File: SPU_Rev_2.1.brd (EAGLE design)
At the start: 127.6 x 101.6 mm, 251 parts, among them Q1 12MHz

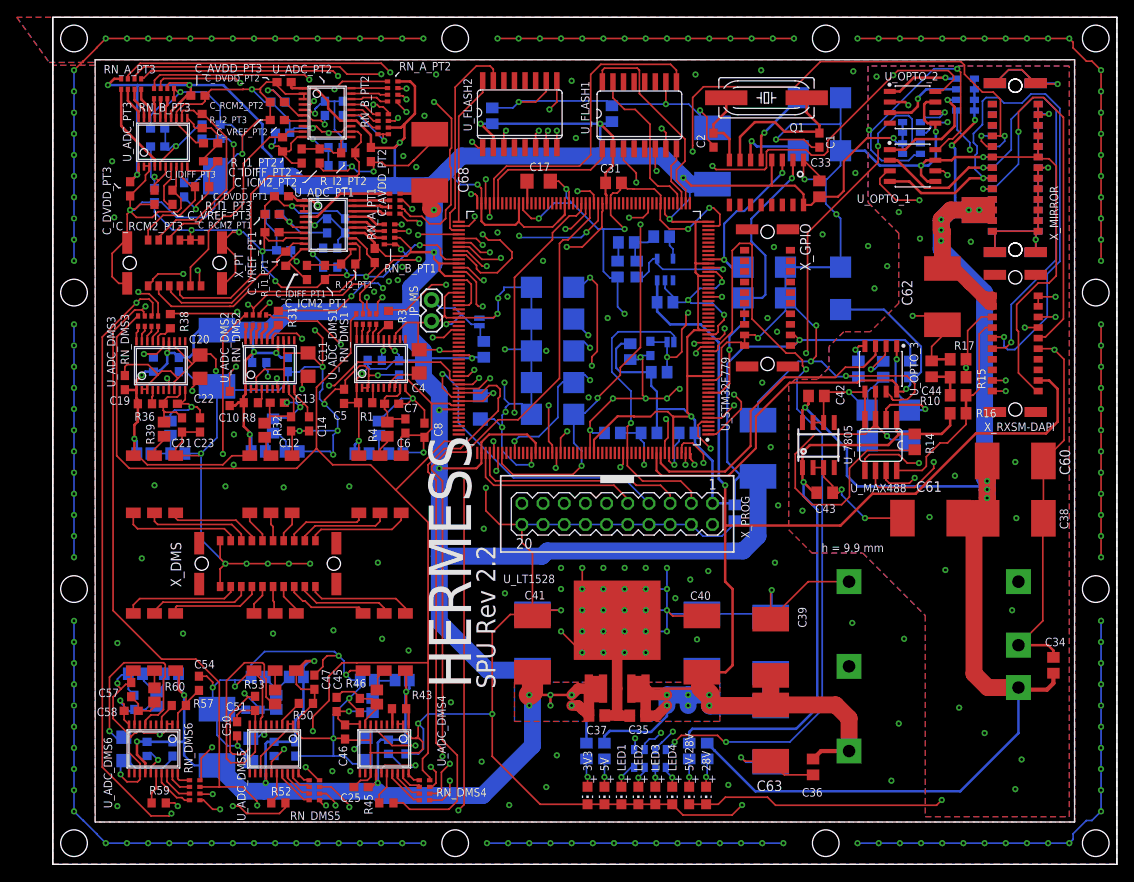
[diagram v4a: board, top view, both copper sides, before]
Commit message: microsd added
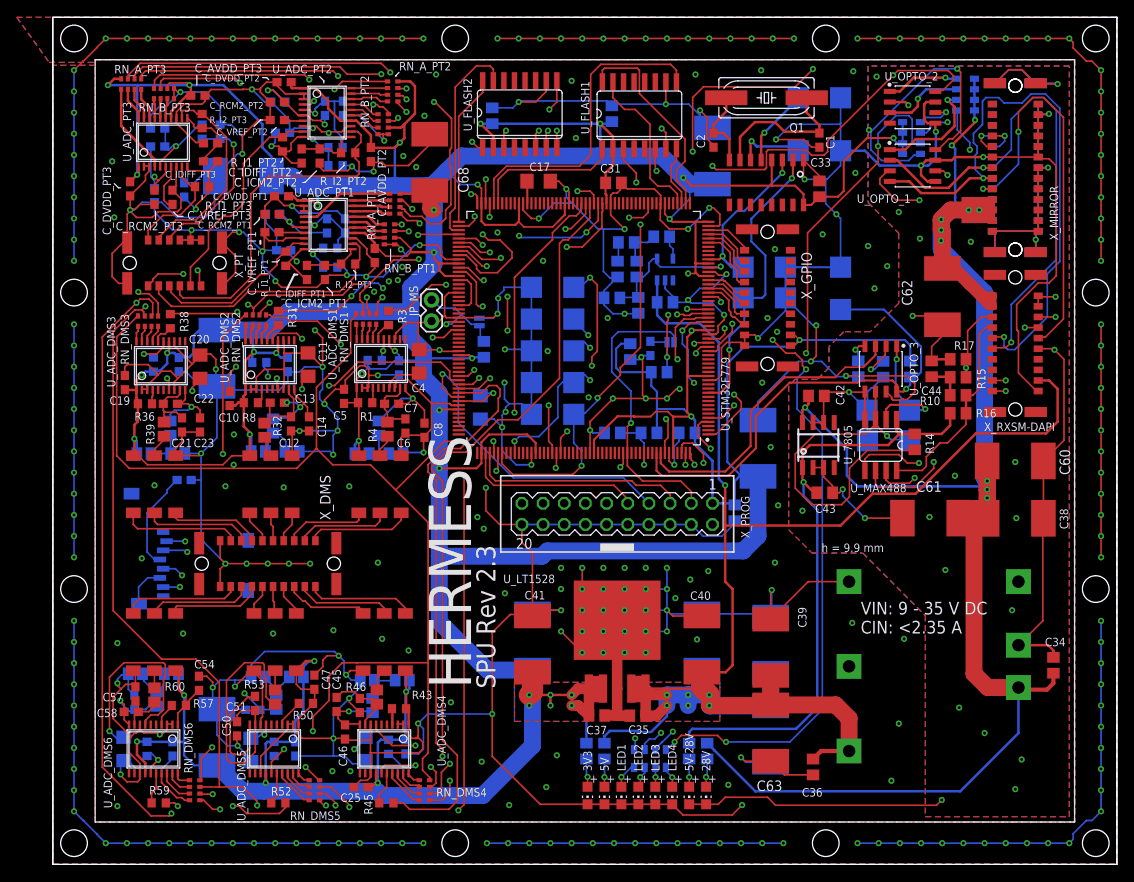
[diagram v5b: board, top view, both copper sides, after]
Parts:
- added C74: 10n, rcl:C0805
- added C75: 100n, rcl:C0805
- added C76: 100n, aSparkFun:0603-CAP
- added U$7: MICROSD, adafruit:MICROSD
- moved C57 0.72 mm to (15.0, 20.4)
- moved C58 0.13 mm to (14.5, 18.3)
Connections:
- new net IO1: U_STM32F779.50, X_GPIO.P$A10
- new net IO2: U_STM32F779.49, X_GPIO.P$A9
- new net IO3: U_STM32F779.48, X_GPIO.P$A8
- new net IO4: U_STM32F779.47, X_GPIO.P$A7
- new net IO5: U_STM32F779.38, X_GPIO.P$A6
- new net IO6: U_STM32F779.37, X_GPIO.P$A5
- new net IO7: U_STM32F779.36, X_GPIO.P$A4
- new net IO8: U_STM32F779.35, X_GPIO.P$A3
- new net SD_CS: U$7.2, U_STM32F779.31
- new net SPI5_MISO: U$7.7, U_STM32F779.29
- new net SPI5_MOSI: U$7.3, U_STM32F779.30
- new net SPI5_SCK: U$7.5, U_STM32F779.28
- net 3V3: now also C76.1, U$7.4
- net 3V3REF: now also C74.2, C75.2
- net GND: now also C74.1, C75.1, C76.2, U$7.6, U$7.MT1, U$7.MT2
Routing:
- net SPI5_SCK: track 0.00 -> 95.4 mm, vias 0 -> 3
- net SPI5_MISO: track 0.00 -> 89.1 mm, vias 0 -> 3
- net SD_CS: track 0.00 -> 82.4 mm, vias 0 -> 2
- net SPI5_MOSI: track 0.00 -> 82.4 mm, vias 0 -> 2
- net LED_4: track 98.8 -> 81.3 mm, vias 3 -> 5
- net 3V3: track 862.8 -> 877.4 mm, vias 39 -> 41
- net GND: track 1440.1 -> 1454.0 mm
- net IO4: track 0.00 -> 7.74 mm
- net IO8: track 0.00 -> 6.83 mm
- net IO3: track 0.00 -> 6.78 mm
- net IO7: track 0.00 -> 6.36 mm
- net IO2: track 0.00 -> 6.26 mm
- net IO1: track 0.00 -> 5.57 mm
- net IO6: track 0.00 -> 5.33 mm
- net IO5: track 0.00 -> 4.96 mm
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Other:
- board text added: "SPU Rev 2.3"
- board text added: "VIN: 9 - 35 V DC CIN: <2.35 A"
- board text removed: "SPU Rev 2.2"

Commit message: foo
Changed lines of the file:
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@@
 <drawing>
 <settings>
-<setting alwaysvectorfont="no"/>
+<setting alwaysvectorfont="yes"/>
 <setting verticaltext="up"/>
 </settings>
@@
 <wire x1="15.416" y1="30.783" x2="15.416" y2="31.261" width="0.2032" layer="16"/>
 <wire x1="16.454" y1="34.361" x2="15.367" y2="33.274" width="0.2032" layer="16"/>
-<wire x1="99.568" y1="91.948" x2="101.092" y2="95.123" width="0" layer="19" extent="16-16"/>
-<wire x1="64.4398" y1="61.5696" x2="62.484" y2="61.595" width="0" layer="19" extent="16-16"/>
-<wire x1="40.767" y1="11.176" x2="41.187" y2="9.271" width="0" layer="19" extent="1-1"/>
-<wire x1="71.628" y1="65.532" x2="73.66" y2="66.04" width="0" layer="19" extent="1-1"/>
-<wire x1="12.446" y1="77.597" x2="14.351" y2="78.486" width="0" layer="19" extent="1-1"/>
-<wire x1="38.608" y1="11.176" x2="40.767" y2="11.176" width="0" layer="19" extent="1-1"/>
-<wire x1="91.948" y1="63.881" x2="89.662" y2="63.119" width="0" layer="19" extent="1-1"/>
-<wire x1="90.805" y1="65.532" x2="91.948" y2="63.881" width="0" layer="19" extent="1-1"/>
-<wire x1="91.694" y1="73.787" x2="92.964" y2="71.628" width="0" layer="19" extent="16-16"/>
-<wire x1="97.409" y1="75.565" x2="99.06" y2="77.978" width="0" layer="19" extent="1-1"/>
-<wire x1="86.106" y1="9.525" x2="87.757" y2="7.112" width="0" layer="19" extent="1-1"/>
-<wire x1="67.31" y1="93.98" x2="64.262" y2="94.0054" width="0" layer="19" extent="1-1"/>
-<wire x1="38.735" y1="28.067" x2="39.37" y2="25.019" width="0" layer="19" extent="1-1"/>
-<wire x1="101.346" y1="82.931" x2="99.568" y2="85.598" width="0" layer="19" extent="16-16"/>
-<wire x1="91.694" y1="36.195" x2="91.313" y2="32.893" width="0" layer="19" extent="1-1"/>
-<wire x1="63.881" y1="72.39" x2="62.484" y2="69.215" width="0" layer="19" extent="16-16"/>
-<wire x1="91.186" y1="50.038" x2="89.662" y2="53.286" width="0" layer="19" extent="16-16"/>
-<wire x1="82.169" y1="94.742" x2="78.613" y2="93.8784" width="0" layer="19" extent="1-1"/>
-<wire x1="12.827" y1="26.543" x2="14.732" y2="23.239" width="0" layer="19" extent="1-1"/>
-<wire x1="12.827" y1="6.985" x2="13.208" y2="10.795" width="0" layer="19" extent="1-1"/>
-<wire x1="12.192" y1="84.328" x2="16.013" y2="83.6962" width="0" layer="19" extent="1-1"/>
-<wire x1="32.766" y1="45.212" x2="33.782" y2="49.024" width="0" layer="19" extent="1-1"/>
-<wire x1="26.797" y1="51.562" x2="22.733" y2="51.855" width="0" layer="19" extent="1-1"/>
-<wire x1="59.309" y1="32.512" x2="62.611" y2="30.045" width="0" layer="19" extent="16-16"/>
-<wire x1="102.87" y1="74.168" x2="99.568" y2="71.628" width="0" layer="19" extent="16-16"/>
-<wire x1="105.156" y1="71.755" x2="102.87" y2="74.168" width="0" layer="19" extent="1-1"/>
-<wire x1="103.632" y1="69.088" x2="105.156" y2="71.755" width="0" layer="19" extent="1-1"/>
-<wire x1="25.781" y1="45.339" x2="21.678" y2="46.101" width="0" layer="19" extent="16-16"/>
-<wire x1="40.64" y1="45.339" x2="38.7096" y2="49.149" width="0" layer="19" extent="1-1"/>
-<wire x1="17.272" y1="45.466" x2="19.812" y2="49.024" width="0" layer="19" extent="1-1"/>
-<wire x1="14.516" y1="44.461" x2="17.272" y2="45.466" width="0" layer="19" extent="16-16"/>
-<wire x1="44.577" y1="27.051" x2="42.291" y2="23.239" width="0" layer="19" extent="1-1"/>
-<wire x1="47.752" y1="25.654" x2="44.577" y2="27.051" width="0" layer="19" extent="1-1"/>
-<wire x1="90.17" y1="57.785" x2="89.662" y2="53.286" width="0" layer="19" extent="16-16"/>
-<wire x1="56.769" y1="40.259" x2="61.341" y2="40.767" width="0" layer="19" extent="1-1"/>
-<wire x1="52.832" y1="19.431" x2="48.895" y2="16.891" width="0" layer="19" extent="1-1"/>
-<wire x1="100.965" y1="28.956" x2="100.584" y2="33.909" width="0" layer="19" extent="1-1"/>
-<wire x1="83.693" y1="35.179" x2="78.74" y2="35.56" width="0" layer="19" extent="1-1"/>
-<wire x1="31.496" y1="27.686" x2="29.21" y2="23.239" width="0" layer="19" extent="1-1"/>
-<wire x1="64.262" y1="9.271" x2="69.215" y2="7.205" width="0" layer="19" extent="1-1"/>
-<wire x1="65.532" y1="13.081" x2="64.262" y2="9.271" width="0" layer="19" extent="1-1"/>
-<wire x1="59.817" y1="7.112" x2="64.262" y2="9.271" width="0" layer="19" extent="1-1"/>
-<wire x1="15.416" y1="31.261" x2="12.827" y2="26.543" width="0" layer="19" extent="16-16"/>
-<wire x1="15.748" y1="36.703" x2="17.916" y2="34.361" width="0" layer="19" extent="16-16"/>
-<wire x1="20.701" y1="27.686" x2="22.606" y2="22.567" width="0" layer="19" extent="1-1"/>
-<wire x1="92.075" y1="43.053" x2="86.868" y2="41.214" width="0" layer="19" extent="16-16"/>
-<wire x1="56.515" y1="12.319" x2="57.785" y2="18.034" width="0" layer="19" extent="1-1"/>
-<wire x1="107.188" y1="27.051" x2="100.965" y2="28.956" width="0" layer="19" extent="1-1"/>
-<wire x1="51.054" y1="94.742" x2="50.292" y2="87.576" width="0" layer="19" extent="1-1"/>
-<wire x1="90.043" y1="95.25" x2="82.169" y2="94.742" width="0" layer="19" extent="1-1"/>
-<wire x1="44.069" y1="36.195" x2="35.941" y2="36.068" width="0" layer="19" extent="1-1"/>
-<wire x1="105.664" y1="10.033" x2="96.266" y2="10.734" width="0" layer="19" extent="1-1"/>
-<wire x1="106.553" y1="16.891" x2="105.664" y2="10.033" width="0" layer="19" extent="1-1"/>
 </signal>
 <signal name="28V">
@@
 <wire x1="96.393" y1="44.577" x2="95.123" y2="45.847" width="0.3048" layer="1"/>
 <wire x1="94.996" y1="47.592" x2="94.996" y2="49.403" width="0.3048" layer="1"/>
-<wire x1="106.614" y1="51.623" x2="108.458" y2="51.623" width="0.3048" layer="1"/>
+<wire x1="106.614" y1="51.623" x2="106.868" y2="51.623" width="0.3048" layer="1"/>
+<wire x1="106.868" y1="51.623" x2="108.458" y2="51.623" width="0.3048" layer="1"/>
 <wire x1="94.996" y1="49.403" x2="95.885" y2="50.292" width="0.3048" layer="1"/>
-<wire x1="95.885" y1="50.292" x2="105.283" y2="50.292" width="0.3048" layer="1"/>
-<wire x1="105.283" y1="50.292" x2="106.614" y2="51.623" width="0.3048" layer="1"/>
+<wire x1="95.885" y1="50.292" x2="105.537" y2="50.292" width="0.3048" layer="1"/>
+<wire x1="105.537" y1="50.292" x2="106.868" y2="51.623" width="0.3048" layer="1"/>
 <wire x1="106.299" y1="53.3654" x2="106.299" y2="51.938" width="0.3048" layer="1"/>
 <wire x1="106.299" y1="51.938" x2="106.614" y2="51.623" width="0.3048" layer="1"/>

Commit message: bar
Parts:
- moved C76 10.5 mm to (12.7, 52.7), turned to 90 degrees
- moved U$7 5.22 mm to (27.3, 35.8)
- moved R41 3.56 mm to (16.1, 52.8)
- moved R42 1.92 mm to (20.3, 51.2)
- moved R40 1.55 mm to (19.4, 53.8)
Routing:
- net SPI5_SCK: track 95.4 -> 100.6 mm
- net SPI5_MISO: track 89.1 -> 94.1 mm
- net SPI5_MOSI: track 82.4 -> 87.2 mm
- net SD_CS: track 82.4 -> 87.2 mm
- net 3V3: track 877.4 -> 880.3 mm
- net N$91: track 9.95 -> 8.66 mm
- net GND: track 1454.0 -> 1454.6 mm, vias 168 -> 169

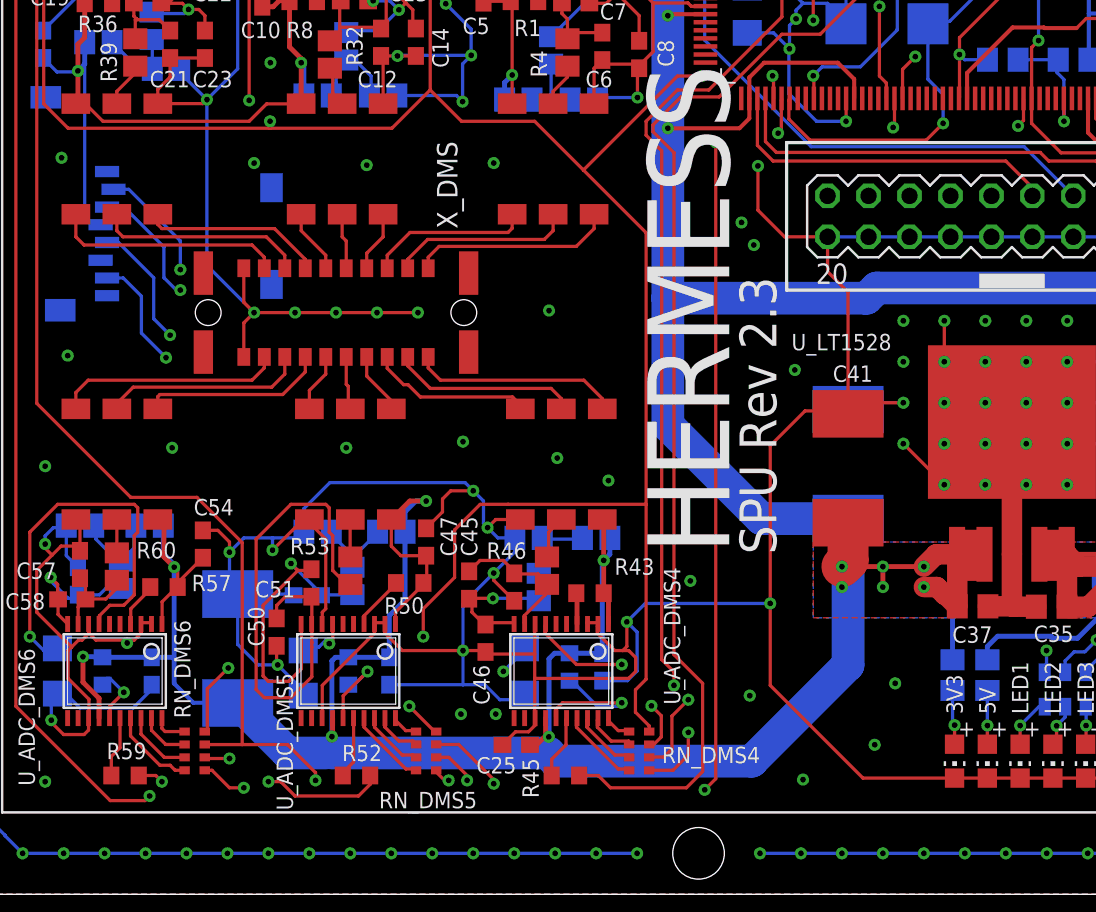
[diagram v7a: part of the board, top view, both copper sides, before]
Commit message: added LWL OUT
added LWL OUT jack
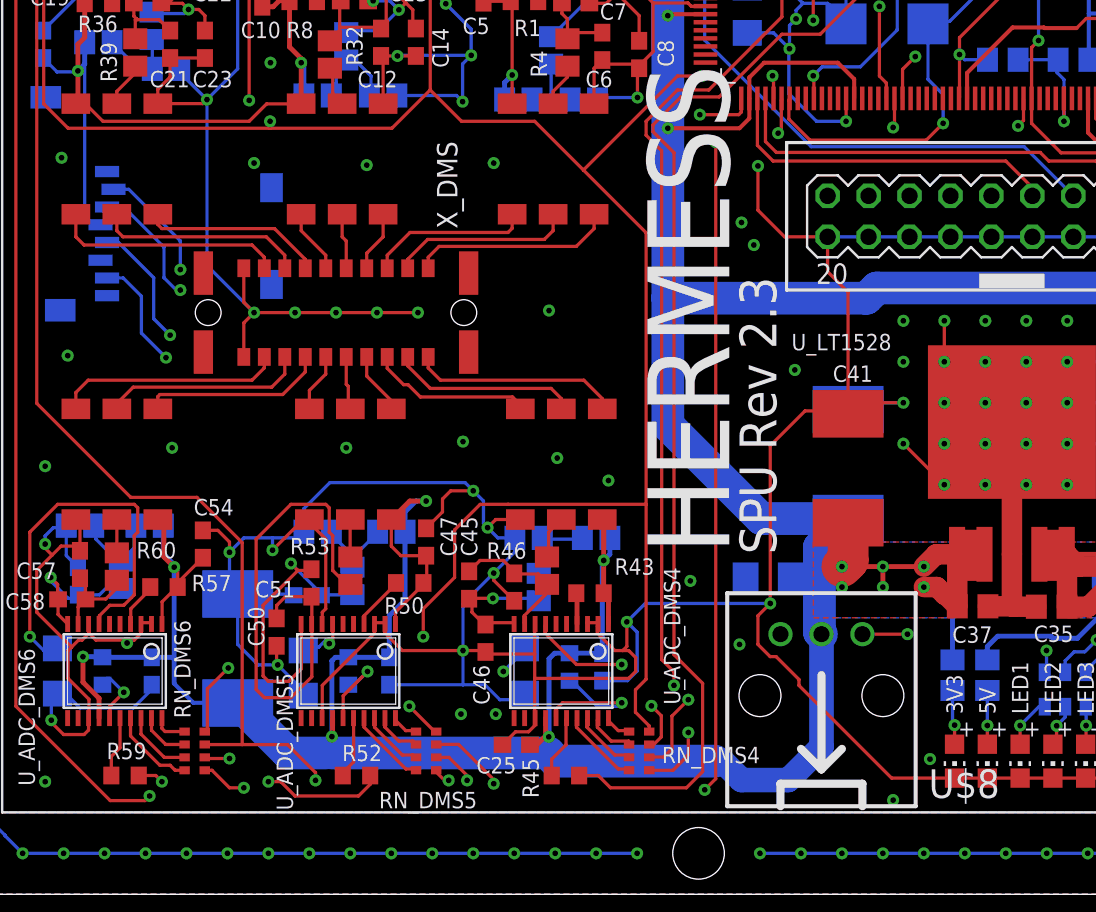
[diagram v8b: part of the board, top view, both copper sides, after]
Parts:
- added C77: (no value), rcl:C1206
- added U$8: PLT131PLT131-T1, everlight-fiber-optics-spdif:PLT131-T1
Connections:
- new net LWL_OUT: U$8.VIN, U_STM32F779.157
- net 3V3: now also C77.1, U$8.VCC
- net GND: now also C77.2, U$8.GND
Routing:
- net LWL_OUT: track 0.00 -> 37.8 mm, vias 0 -> 1
- net 3V3: track 880.3 -> 887.6 mm
- net GND: track 1454.6 -> 1457.2 mm
